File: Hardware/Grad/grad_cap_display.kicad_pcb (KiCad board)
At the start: 2 copper layers, 0 parts

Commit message: Start of modular PCB
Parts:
- added C1001: 1uF, New_Library:Worthington_C_0603, F.Cu at (-409.5, 120.0)
- added C1002: 22uF, New_Library:Worthington_C_0603, F.Cu at (-409.5, 122.5)
- added C1003: 1uF, New_Library:Worthington_C_0603, F.Cu at (-409.5, 125.0)
- added C1004: 22uF, New_Library:Worthington_C_0603, F.Cu at (-409.5, 127.5)
- added C1005: 100nF, New_Library:Worthington_C_0402, F.Cu at (-409.8, 149.9)
- added C1006: 22uF, New_Library:Worthington_C_0603, F.Cu at (-409.5, 130.0)
- added C1007: 100nF, New_Library:Worthington_C_0402, F.Cu at (-409.8, 152.1)
- added C1008: 100nF, New_Library:Worthington_C_0402, F.Cu at (-409.8, 154.3)
- added C1009: 100nF, New_Library:Worthington_C_0402, F.Cu at (-409.8, 156.5)
- added C1010: 100nF, New_Library:Worthington_C_0402, F.Cu at (-409.8, 158.7)
- added C1011: 100nF, New_Library:Worthington_C_0402, F.Cu at (-406.6, 149.9)
- added C1012: 22uF, New_Library:Worthington_D_0603, F.Cu at (-409.4, 135.0)
- added C1013: 100nF, New_Library:Worthington_C_0402, F.Cu at (-406.6, 152.1)
- added C1014: 100nF, New_Library:Worthington_C_0402, F.Cu at (-406.6, 154.3)
- added C1015: 22uF, New_Library:Worthington_C_0603, F.Cu at (-409.5, 132.5)
- added C1016: 100nF, New_Library:Worthington_C_0402, F.Cu at (-406.6, 156.5)
- added C1101: 100nF, Capacitor_SMD:C_0402_1005Metric, F.Cu at (-379.2, 157.2)
- added C1102: 22uF, Capacitor_SMD:C_0603_1608Metric, F.Cu at (-391.2, 160.4)
- added C1103: 22uF, Capacitor_SMD:C_0603_1608Metric, F.Cu at (-391.2, 163.0)
- added C1104: 100nF, Capacitor_SMD:C_0402_1005Metric, F.Cu at (-379.2, 159.2)
- added C1105: 100nF, Capacitor_SMD:C_0402_1005Metric, F.Cu at (-379.2, 161.2)
- added C1106: 22uF, Capacitor_SMD:C_0603_1608Metric, F.Cu at (-391.2, 165.5)
- added C201: 1uF, New_Library:Worthington_C_0603, F.Cu at (-268.5, 5.08)
- added C202: 22uF, New_Library:Worthington_C_0603, F.Cu at (-268.5, 7.58)
- added C203: 1uF, New_Library:Worthington_C_0603, F.Cu at (-268.5, 10.1)
- added C204: 22uF, New_Library:Worthington_C_0603, F.Cu at (-268.5, 12.6)
- added C205: 100nF, New_Library:Worthington_C_0402, F.Cu at (-268.8, 34.9)
- added C206: 22uF, New_Library:Worthington_C_0603, F.Cu at (-268.5, 15.1)
- added C207: 100nF, New_Library:Worthington_C_0402, F.Cu at (-268.8, 37.1)
- added C208: 100nF, New_Library:Worthington_C_0402, F.Cu at (-268.8, 39.3)
- added C209: 100nF, New_Library:Worthington_C_0402, F.Cu at (-268.8, 41.5)
- added C210: 100nF, New_Library:Worthington_C_0402, F.Cu at (-268.8, 43.7)
- added C211: 100nF, New_Library:Worthington_C_0402, F.Cu at (-265.6, 34.9)
- added C212: 22uF, New_Library:Worthington_D_0603, F.Cu at (-268.4, 20.1)
- added C213: 100nF, New_Library:Worthington_C_0402, F.Cu at (-265.6, 37.1)
- added C214: 100nF, New_Library:Worthington_C_0402, F.Cu at (-265.6, 39.3)
- added C215: 22uF, New_Library:Worthington_C_0603, F.Cu at (-268.5, 17.6)
- added C216: 100nF, New_Library:Worthington_C_0402, F.Cu at (-265.6, 41.5)
- added C301: 1uF, New_Library:Worthington_C_0603, F.Cu at (-409.5, 3.98)
- added C302: 22uF, New_Library:Worthington_C_0603, F.Cu at (-409.5, 6.49)
- added C303: 1uF, New_Library:Worthington_C_0603, F.Cu at (-409.5, 8.98)
- added C304: 22uF, New_Library:Worthington_C_0603, F.Cu at (-409.5, 11.5)
- added C305: 100nF, New_Library:Worthington_C_0402, F.Cu at (-409.8, 33.8)
- added C306: 22uF, New_Library:Worthington_C_0603, F.Cu at (-409.5, 14.0)
- added C307: 100nF, New_Library:Worthington_C_0402, F.Cu at (-409.8, 36.0)
- added C308: 100nF, New_Library:Worthington_C_0402, F.Cu at (-409.8, 38.2)
- added C309: 100nF, New_Library:Worthington_C_0402, F.Cu at (-409.8, 40.4)
- added C310: 100nF, New_Library:Worthington_C_0402, F.Cu at (-409.8, 42.6)
- added C311: 100nF, New_Library:Worthington_C_0402, F.Cu at (-406.6, 33.8)
- added C312: 22uF, New_Library:Worthington_D_0603, F.Cu at (-409.4, 19.0)
- added C313: 100nF, New_Library:Worthington_C_0402, F.Cu at (-406.6, 36.0)
- added C314: 100nF, New_Library:Worthington_C_0402, F.Cu at (-406.6, 38.2)
- added C315: 22uF, New_Library:Worthington_C_0603, F.Cu at (-409.5, 16.5)
- added C316: 100nF, New_Library:Worthington_C_0402, F.Cu at (-406.6, 40.4)
- added C401: 1uF, New_Library:Worthington_C_0603, F.Cu at (-409.5, 62.0)
- added C402: 22uF, New_Library:Worthington_C_0603, F.Cu at (-409.5, 64.5)
- added C403: 1uF, New_Library:Worthington_C_0603, F.Cu at (-409.5, 67.0)
- added C404: 22uF, New_Library:Worthington_C_0603, F.Cu at (-409.5, 69.5)
- added C405: 100nF, New_Library:Worthington_C_0402, F.Cu at (-409.8, 91.9)
- added C406: 22uF, New_Library:Worthington_C_0603, F.Cu at (-409.5, 72.0)
- added C407: 100nF, New_Library:Worthington_C_0402, F.Cu at (-409.8, 94.1)
- added C408: 100nF, New_Library:Worthington_C_0402, F.Cu at (-409.8, 96.3)
- added C409: 100nF, New_Library:Worthington_C_0402, F.Cu at (-409.8, 98.5)
- added C410: 100nF, New_Library:Worthington_C_0402, F.Cu at (-409.8, 100.7)
- added C411: 100nF, New_Library:Worthington_C_0402, F.Cu at (-406.6, 91.9)
- added C412: 22uF, New_Library:Worthington_D_0603, F.Cu at (-409.4, 77.0)
- added C413: 100nF, New_Library:Worthington_C_0402, F.Cu at (-406.6, 94.1)
- added C414: 100nF, New_Library:Worthington_C_0402, F.Cu at (-406.6, 96.3)
- added C415: 22uF, New_Library:Worthington_C_0603, F.Cu at (-409.5, 74.5)
- added C416: 100nF, New_Library:Worthington_C_0402, F.Cu at (-406.6, 98.5)
- added C501: 1uF, New_Library:Worthington_C_0603, F.Cu at (-467.0, 3.98)
- added C502: 22uF, New_Library:Worthington_C_0603, F.Cu at (-467.0, 6.49)
- added C503: 1uF, New_Library:Worthington_C_0603, F.Cu at (-467.0, 8.98)
- added C504: 22uF, New_Library:Worthington_C_0603, F.Cu at (-467.0, 11.5)
- added C505: 100nF, New_Library:Worthington_C_0402, F.Cu at (-467.3, 33.8)
- added C506: 22uF, New_Library:Worthington_C_0603, F.Cu at (-467.0, 14.0)
- added C507: 100nF, New_Library:Worthington_C_0402, F.Cu at (-467.3, 36.0)
- added C508: 100nF, New_Library:Worthington_C_0402, F.Cu at (-467.3, 38.2)
- added C509: 100nF, New_Library:Worthington_C_0402, F.Cu at (-467.3, 40.4)
- added C510: 100nF, New_Library:Worthington_C_0402, F.Cu at (-467.3, 42.6)
- added C511: 100nF, New_Library:Worthington_C_0402, F.Cu at (-464.1, 33.8)
- added C512: 22uF, New_Library:Worthington_D_0603, F.Cu at (-466.9, 19.0)
- added C513: 100nF, New_Library:Worthington_C_0402, F.Cu at (-464.1, 36.0)
- added C514: 100nF, New_Library:Worthington_C_0402, F.Cu at (-464.1, 38.2)
- added C515: 22uF, New_Library:Worthington_C_0603, F.Cu at (-467.0, 16.5)
- added C516: 100nF, New_Library:Worthington_C_0402, F.Cu at (-464.1, 40.4)
- added C601: 1uF, New_Library:Worthington_C_0603, F.Cu at (-524.4, 62.0)
- added C602: 22uF, New_Library:Worthington_C_0603, F.Cu at (-524.4, 64.5)
- added C603: 1uF, New_Library:Worthington_C_0603, F.Cu at (-524.4, 67.0)
- added C604: 22uF, New_Library:Worthington_C_0603, F.Cu at (-524.4, 69.5)
- added C605: 100nF, New_Library:Worthington_C_0402, F.Cu at (-524.7, 91.9)
- added C606: 22uF, New_Library:Worthington_C_0603, F.Cu at (-524.4, 72.0)
- added C607: 100nF, New_Library:Worthington_C_0402, F.Cu at (-524.7, 94.1)
- added C608: 100nF, New_Library:Worthington_C_0402, F.Cu at (-524.7, 96.3)
- added C609: 100nF, New_Library:Worthington_C_0402, F.Cu at (-524.7, 98.5)
- added C610: 100nF, New_Library:Worthington_C_0402, F.Cu at (-524.7, 100.7)
- added C611: 100nF, New_Library:Worthington_C_0402, F.Cu at (-521.5, 91.9)
- added C612: 22uF, New_Library:Worthington_D_0603, F.Cu at (-524.3, 77.0)
- added C613: 100nF, New_Library:Worthington_C_0402, F.Cu at (-521.5, 94.1)
- added C614: 100nF, New_Library:Worthington_C_0402, F.Cu at (-521.5, 96.3)
- added C615: 22uF, New_Library:Worthington_C_0603, F.Cu at (-524.4, 74.5)
- added C616: 100nF, New_Library:Worthington_C_0402, F.Cu at (-521.5, 98.5)
- added C701: 1uF, New_Library:Worthington_C_0603, F.Cu at (-467.0, 62.0)
- added C702: 22uF, New_Library:Worthington_C_0603, F.Cu at (-467.0, 64.5)
- added C703: 1uF, New_Library:Worthington_C_0603, F.Cu at (-467.0, 67.0)
- added C704: 22uF, New_Library:Worthington_C_0603, F.Cu at (-467.0, 69.5)
- added C705: 100nF, New_Library:Worthington_C_0402, F.Cu at (-467.3, 91.9)
- added C706: 22uF, New_Library:Worthington_C_0603, F.Cu at (-467.0, 72.0)
- added C707: 100nF, New_Library:Worthington_C_0402, F.Cu at (-467.3, 94.1)
- added C708: 100nF, New_Library:Worthington_C_0402, F.Cu at (-467.3, 96.3)
- added C709: 100nF, New_Library:Worthington_C_0402, F.Cu at (-467.3, 98.5)
- added C710: 100nF, New_Library:Worthington_C_0402, F.Cu at (-467.3, 100.7)
- added C711: 100nF, New_Library:Worthington_C_0402, F.Cu at (-464.1, 91.9)
- added C712: 22uF, New_Library:Worthington_D_0603, F.Cu at (-466.9, 77.0)
- added C713: 100nF, New_Library:Worthington_C_0402, F.Cu at (-464.1, 94.1)
- added C714: 100nF, New_Library:Worthington_C_0402, F.Cu at (-464.1, 96.3)
- added C715: 22uF, New_Library:Worthington_C_0603, F.Cu at (-467.0, 74.5)
- added C716: 100nF, New_Library:Worthington_C_0402, F.Cu at (-464.1, 98.5)
- added C801: 1uF, New_Library:Worthington_C_0603, F.Cu at (-467.0, 120.0)
- added C802: 22uF, New_Library:Worthington_C_0603, F.Cu at (-467.0, 122.5)
- added C803: 1uF, New_Library:Worthington_C_0603, F.Cu at (-467.0, 125.0)
- added C804: 22uF, New_Library:Worthington_C_0603, F.Cu at (-467.0, 127.5)
- added C805: 100nF, New_Library:Worthington_C_0402, F.Cu at (-467.3, 149.9)
- added C806: 22uF, New_Library:Worthington_C_0603, F.Cu at (-467.0, 130.0)
- added C807: 100nF, New_Library:Worthington_C_0402, F.Cu at (-467.3, 152.1)
- added C808: 100nF, New_Library:Worthington_C_0402, F.Cu at (-467.3, 154.3)
- added C809: 100nF, New_Library:Worthington_C_0402, F.Cu at (-467.3, 156.5)
- added C810: 100nF, New_Library:Worthington_C_0402, F.Cu at (-467.3, 158.7)
- added C811: 100nF, New_Library:Worthington_C_0402, F.Cu at (-464.1, 149.9)
- added C812: 22uF, New_Library:Worthington_D_0603, F.Cu at (-466.9, 135.0)
- added C813: 100nF, New_Library:Worthington_C_0402, F.Cu at (-464.1, 152.1)
- added C814: 100nF, New_Library:Worthington_C_0402, F.Cu at (-464.1, 154.3)
- added C815: 22uF, New_Library:Worthington_C_0603, F.Cu at (-467.0, 132.5)
- added C816: 100nF, New_Library:Worthington_C_0402, F.Cu at (-464.1, 156.5)
- added C901: 1uF, New_Library:Worthington_C_0603, F.Cu at (-524.4, 120.0)
- added C902: 22uF, New_Library:Worthington_C_0603, F.Cu at (-524.4, 122.5)
- added C903: 1uF, New_Library:Worthington_C_0603, F.Cu at (-524.4, 125.0)
- added C904: 22uF, New_Library:Worthington_C_0603, F.Cu at (-524.4, 127.5)
- added C905: 100nF, New_Library:Worthington_C_0402, F.Cu at (-524.7, 149.9)
- added C906: 22uF, New_Library:Worthington_C_0603, F.Cu at (-524.4, 130.0)
- added C907: 100nF, New_Library:Worthington_C_0402, F.Cu at (-524.7, 152.1)
- added C908: 100nF, New_Library:Worthington_C_0402, F.Cu at (-524.7, 154.3)
- added C909: 100nF, New_Library:Worthington_C_0402, F.Cu at (-524.7, 156.5)
- added C910: 100nF, New_Library:Worthington_C_0402, F.Cu at (-524.7, 158.7)
- added C911: 100nF, New_Library:Worthington_C_0402, F.Cu at (-521.5, 149.9)
- added C912: 22uF, New_Library:Worthington_D_0603, F.Cu at (-524.3, 135.0)
- added C913: 100nF, New_Library:Worthington_C_0402, F.Cu at (-521.5, 152.1)
- added C914: 100nF, New_Library:Worthington_C_0402, F.Cu at (-521.5, 154.3)
- added C915: 22uF, New_Library:Worthington_C_0603, F.Cu at (-524.4, 132.5)
- added C916: 100nF, New_Library:Worthington_C_0402, F.Cu at (-521.5, 156.5)
- added D1001: LED_Small, New_Library:Worthington_LED_0603, F.Cu at (-409.4, 137.5)
- added D1002: RED, New_Library:Worthington_LED_0603, F.Cu at (-409.4, 140.0)
- added D1003: RED, New_Library:Worthington_LED_0603, F.Cu at (-409.4, 142.5)
- added D1004: RED, New_Library:Worthington_LED_0603, F.Cu at (-409.4, 145.0)
- added D1005: RED, New_Library:Worthington_LED_0603, F.Cu at (-409.4, 147.5)
- added D1101: LED_Small, New_Library:Worthington_LED_0603, F.Cu at (-375.5, 162.8)
- added D1102: LED_Small, New_Library:Worthington_LED_0603, F.Cu at (-375.5, 165.3)
- added D201: LED_Small, New_Library:Worthington_LED_0603, F.Cu at (-268.4, 22.6)
- added D202: RED, New_Library:Worthington_LED_0603, F.Cu at (-268.4, 25.1)
- added D203: RED, New_Library:Worthington_LED_0603, F.Cu at (-268.4, 27.6)
- added D204: RED, New_Library:Worthington_LED_0603, F.Cu at (-268.4, 30.1)
- added D205: RED, New_Library:Worthington_LED_0603, F.Cu at (-268.4, 32.6)
- added D301: LED_Small, New_Library:Worthington_LED_0603, F.Cu at (-409.4, 21.5)
- added D302: RED, New_Library:Worthington_LED_0603, F.Cu at (-409.4, 24.0)
- added D303: RED, New_Library:Worthington_LED_0603, F.Cu at (-409.4, 26.5)
- added D304: RED, New_Library:Worthington_LED_0603, F.Cu at (-409.4, 29.0)
- added D305: RED, New_Library:Worthington_LED_0603, F.Cu at (-409.4, 31.5)
- added D401: LED_Small, New_Library:Worthington_LED_0603, F.Cu at (-409.4, 79.5)
- added D402: RED, New_Library:Worthington_LED_0603, F.Cu at (-409.4, 82.0)
- added D403: RED, New_Library:Worthington_LED_0603, F.Cu at (-409.4, 84.5)
- added D404: RED, New_Library:Worthington_LED_0603, F.Cu at (-409.4, 87.0)
- added D405: RED, New_Library:Worthington_LED_0603, F.Cu at (-409.4, 89.5)
- added D501: LED_Small, New_Library:Worthington_LED_0603, F.Cu at (-466.9, 21.5)
- added D502: RED, New_Library:Worthington_LED_0603, F.Cu at (-466.9, 24.0)
- added D503: RED, New_Library:Worthington_LED_0603, F.Cu at (-466.9, 26.5)
- added D504: RED, New_Library:Worthington_LED_0603, F.Cu at (-466.9, 29.0)
- added D505: RED, New_Library:Worthington_LED_0603, F.Cu at (-466.9, 31.5)
- added D601: LED_Small, New_Library:Worthington_LED_0603, F.Cu at (-524.3, 79.5)
- added D602: RED, New_Library:Worthington_LED_0603, F.Cu at (-524.3, 82.0)
- added D603: RED, New_Library:Worthington_LED_0603, F.Cu at (-524.3, 84.5)
- added D604: RED, New_Library:Worthington_LED_0603, F.Cu at (-524.3, 87.0)
- added D605: RED, New_Library:Worthington_LED_0603, F.Cu at (-524.3, 89.5)
- added D701: LED_Small, New_Library:Worthington_LED_0603, F.Cu at (-466.9, 79.5)
- added D702: RED, New_Library:Worthington_LED_0603, F.Cu at (-466.9, 82.0)
- added D703: RED, New_Library:Worthington_LED_0603, F.Cu at (-466.9, 84.5)
- added D704: RED, New_Library:Worthington_LED_0603, F.Cu at (-466.9, 87.0)
- added D705: RED, New_Library:Worthington_LED_0603, F.Cu at (-466.9, 89.5)
- added D801: LED_Small, New_Library:Worthington_LED_0603, F.Cu at (-466.9, 137.5)
- added D802: RED, New_Library:Worthington_LED_0603, F.Cu at (-466.9, 140.0)
- added D803: RED, New_Library:Worthington_LED_0603, F.Cu at (-466.9, 142.5)
- added D804: RED, New_Library:Worthington_LED_0603, F.Cu at (-466.9, 145.0)
- added D805: RED, New_Library:Worthington_LED_0603, F.Cu at (-466.9, 147.5)
- added D901: LED_Small, New_Library:Worthington_LED_0603, F.Cu at (-524.3, 137.5)
- added D902: RED, New_Library:Worthington_LED_0603, F.Cu at (-524.3, 140.0)
- added D903: RED, New_Library:Worthington_LED_0603, F.Cu at (-524.3, 142.5)
- added D904: RED, New_Library:Worthington_LED_0603, F.Cu at (-524.3, 145.0)
- added D905: RED, New_Library:Worthington_LED_0603, F.Cu at (-524.3, 147.5)
- added J1001: Amphenol 40-Pin FPC, New_Library:AMPHENOL_62684-402100ALF, F.Cu at (-446.6, 166.6)
- added J101: 6-Pos 2.54mm Header, Connector_PinHeader_2.54mm:PinHeader_1x06_P2.54mm_Vertical, F.Cu at (-400.7, 63.1)
- added J102: 6-Pos 2.54mm Header, Connector_PinHeader_2.54mm:PinHeader_1x06_P2.54mm_Vertical, F.Cu at (-396.1, 63.1)
- added J103: 6-Pos 2.54mm Header, Connector_PinHeader_2.54mm:PinHeader_1x06_P2.54mm_Vertical, F.Cu at (-391.6, 63.1)
- added J104: 6-Pos 2.54mm Header, Connector_PinHeader_2.54mm:PinHeader_1x06_P2.54mm_Vertical, F.Cu at (-387.0, 63.1)
- added J105: 6-Pos 2.54mm Header, Connector_PinHeader_2.54mm:PinHeader_1x06_P2.54mm_Vertical, F.Cu at (-382.4, 63.1)
- added J106: 6-Pos 2.54mm Header, Connector_PinHeader_2.54mm:PinHeader_1x06_P2.54mm_Vertical, F.Cu at (-377.8, 63.1)
- added J107: 6-Pos 2.54mm Header, Connector_PinHeader_2.54mm:PinHeader_1x06_P2.54mm_Vertical, F.Cu at (-373.2, 63.1)
- added J108: 6-Pos 2.54mm Header, Connector_PinHeader_2.54mm:PinHeader_1x06_P2.54mm_Vertical, F.Cu at (-368.6, 63.1)
- added J109: 6-Pos 2.54mm Header, Connector_PinHeader_2.54mm:PinHeader_1x06_P2.54mm_Vertical, F.Cu at (-364.0, 63.1)
- added J1101: JST-PH SPI, Connector_JST:JST_PH_S5B-PH-K_1x05_P2.00mm_Horizontal, F.Cu at (-400.1, 151.9)
- added J1102: JST-PH UART/I2C, Connector_JST:JST_PH_S6B-PH-K_1x06_P2.00mm_Horizontal, F.Cu at (-374.5, 144.6)
- added J1103: JST-PH A#, Connector_JST:JST_PH_S6B-PH-K_1x06_P2.00mm_Horizontal, F.Cu at (-374.5, 154.2)
- added J1104: Micro_SD_Card, New_Library:CUI_MSD-4-A, F.Cu at (-368.4, 128.6)
- added J201: Amphenol 40-Pin FPC, New_Library:AMPHENOL_62684-402100ALF, F.Cu at (-305.5, 51.6)
- added J301: Amphenol 40-Pin FPC, New_Library:AMPHENOL_62684-402100ALF, F.Cu at (-446.6, 50.5)
- added J401: Amphenol 40-Pin FPC, New_Library:AMPHENOL_62684-402100ALF, F.Cu at (-446.6, 108.5)
- added J501: Amphenol 40-Pin FPC, New_Library:AMPHENOL_62684-402100ALF, F.Cu at (-504.0, 50.5)
- added J601: Amphenol 40-Pin FPC, New_Library:AMPHENOL_62684-402100ALF, F.Cu at (-561.5, 108.5)
- added J701: Amphenol 40-Pin FPC, New_Library:AMPHENOL_62684-402100ALF, F.Cu at (-504.0, 108.5)
- added J801: Amphenol 40-Pin FPC, New_Library:AMPHENOL_62684-402100ALF, F.Cu at (-504.0, 166.6)
- added J901: Amphenol 40-Pin FPC, New_Library:AMPHENOL_62684-402100ALF, F.Cu at (-561.5, 166.6)
- added L1001: 22uH, New_Library:CDRH5D28, F.Cu at (-428.4, 165.3)
- added L201: 22uH, New_Library:CDRH5D28, F.Cu at (-287.3, 50.4)
- added L301: 22uH, New_Library:CDRH5D28, F.Cu at (-428.4, 49.3)
- added L401: 22uH, New_Library:CDRH5D28, F.Cu at (-428.4, 107.3)
- added L501: 22uH, New_Library:CDRH5D28, F.Cu at (-485.8, 49.3)
- added L601: 22uH, New_Library:CDRH5D28, F.Cu at (-543.3, 107.3)
- added L701: 22uH, New_Library:CDRH5D28, F.Cu at (-485.8, 107.3)
- added L801: 22uH, New_Library:CDRH5D28, F.Cu at (-485.8, 165.3)
- added L901: 22uH, New_Library:CDRH5D28, F.Cu at (-543.3, 165.3)
- added R1001: 430, New_Library:Worthington_R_0402, F.Cu at (-406.6, 158.7)
- added R1002: 10, Resistor_SMD:R_1210_3225Metric, F.Cu at (-457.7, 172.7)
- added R101: 120, New_Library:Worthington_R_0402, F.Cu at (-401.4, 79.2)
- added R102: 120, New_Library:Worthington_R_0402, F.Cu at (-401.4, 81.4)
- added R1101: 1k, New_Library:Worthington_R_0402, F.Cu at (-367.2, 162.6)
- added R1102: 430, New_Library:Worthington_R_0402, F.Cu at (-367.2, 164.8)
- added R201: 430, New_Library:Worthington_R_0402, F.Cu at (-265.6, 43.7)
- added R202: 10, Resistor_SMD:R_1210_3225Metric, F.Cu at (-316.6, 57.8)
- added R301: 430, New_Library:Worthington_R_0402, F.Cu at (-406.6, 42.6)
- added R302: 10, Resistor_SMD:R_1210_3225Metric, F.Cu at (-457.7, 56.7)
- added R401: 430, New_Library:Worthington_R_0402, F.Cu at (-406.6, 100.7)
- added R402: 10, Resistor_SMD:R_1210_3225Metric, F.Cu at (-457.7, 114.7)
- added R501: 430, New_Library:Worthington_R_0402, F.Cu at (-464.1, 42.6)
- added R502: 10, Resistor_SMD:R_1210_3225Metric, F.Cu at (-515.1, 56.7)
- added R601: 430, New_Library:Worthington_R_0402, F.Cu at (-521.5, 100.7)
- added R602: 10, Resistor_SMD:R_1210_3225Metric, F.Cu at (-572.6, 114.7)
- added R701: 430, New_Library:Worthington_R_0402, F.Cu at (-464.1, 100.7)
- added R702: 10, Resistor_SMD:R_1210_3225Metric, F.Cu at (-515.1, 114.7)
- added R801: 430, New_Library:Worthington_R_0402, F.Cu at (-464.1, 158.7)
- added R802: 10, Resistor_SMD:R_1210_3225Metric, F.Cu at (-515.1, 172.7)
- added R901: 430, New_Library:Worthington_R_0402, F.Cu at (-521.5, 158.7)
- added R902: 10, Resistor_SMD:R_1210_3225Metric, F.Cu at (-572.6, 172.7)
- added RN1001: 10k, New_Library:RESCAXE80P320X160X70-8N, F.Cu at (-412.4, 170.0)
- added RN1002: 430, New_Library:RESCAXE80P320X160X70-8N, F.Cu at (-407.6, 170.0)
- added RN1101: 47k, New_Library:RESCAXE80P320X160X70-8N, F.Cu at (-370.9, 163.9)
- added RN201: 10k, New_Library:RESCAXE80P320X160X70-8N, F.Cu at (-271.4, 55.1)
- added RN202: 430, New_Library:RESCAXE80P320X160X70-8N, F.Cu at (-266.6, 55.1)
- added RN301: 10k, New_Library:RESCAXE80P320X160X70-8N, F.Cu at (-412.4, 54.0)
- added RN302: 430, New_Library:RESCAXE80P320X160X70-8N, F.Cu at (-407.6, 54.0)
- added RN401: 10k, New_Library:RESCAXE80P320X160X70-8N, F.Cu at (-412.4, 112.0)
- added RN402: 430, New_Library:RESCAXE80P320X160X70-8N, F.Cu at (-407.6, 112.0)
- added RN501: 10k, New_Library:RESCAXE80P320X160X70-8N, F.Cu at (-469.9, 54.0)
- added RN502: 430, New_Library:RESCAXE80P320X160X70-8N, F.Cu at (-465.1, 54.0)
- added RN601: 10k, New_Library:RESCAXE80P320X160X70-8N, F.Cu at (-527.3, 112.0)
- added RN602: 430, New_Library:RESCAXE80P320X160X70-8N, F.Cu at (-522.5, 112.0)
- added RN701: 10k, New_Library:RESCAXE80P320X160X70-8N, F.Cu at (-469.9, 112.0)
- added RN702: 430, New_Library:RESCAXE80P320X160X70-8N, F.Cu at (-465.1, 112.0)
- added RN801: 10k, New_Library:RESCAXE80P320X160X70-8N, F.Cu at (-469.9, 170.0)
- added RN802: 430, New_Library:RESCAXE80P320X160X70-8N, F.Cu at (-465.1, 170.0)
- added RN901: 10k, New_Library:RESCAXE80P320X160X70-8N, F.Cu at (-527.3, 170.0)
- added RN902: 430, New_Library:RESCAXE80P320X160X70-8N, F.Cu at (-522.5, 170.0)
- added U1001: LM66200DRLR, Package_TO_SOT_SMD:SOT-583-8, F.Cu at (-453.0, 172.6)
- added U1002: TLV75733PDRV, Package_SON:WSON-6-1EP_2x2mm_P0.65mm_EP1x1.6mm, F.Cu at (-443.7, 172.5)
- added U1003: SN74LVC1G139, Package_SO:VSSOP-8_2.3x2mm_P0.5mm, F.Cu at (-448.4, 172.6)
- added U1004: ESP32-S3-WROOM-1-N8R8, RF_Module:ESP32-S3-WROOM-1, F.Cu at (-436.0, 147.1)
- added U1005: TC7MBL3126CFT, Package_SO:TSSOP-14_4.4x5mm_P0.65mm, F.Cu at (-419.5, 164.5)
- added U1006: AP3019AKTTR, Package_TO_SOT_SMD:TSOT-23-6, F.Cu at (-430.1, 172.0)
- added U1007: W25Q128JVP, Package_SON:WSON-8-1EP_6x5mm_P1.27mm_EP3.4x4.3mm, F.Cu at (-410.9, 164.3)
- added U1008: THVD1400D, Package_SO:SOIC-8_3.9x4.9mm_P1.27mm, F.Cu at (-419.6, 171.1)
- added U1101: TC7MBL3126CFT, Package_SO:TSSOP-14_4.4x5mm_P0.65mm, F.Cu at (-384.7, 153.0)
- added U1102: AZ1117-5.0, Package_TO_SOT_SMD:SOT-223-3_TabPin2, F.Cu at (-398.1, 163.4)
- added U1103: THVD1400D, Package_SO:SOIC-8_3.9x4.9mm_P1.27mm, F.Cu at (-384.9, 159.6)
- added U1104: QTPy SAMD21, New_Library:Py_QT_SAMD21, F.Cu at (-390.3, 137.7)
- added U201: LM66200DRLR, Package_TO_SOT_SMD:SOT-583-8, F.Cu at (-312.0, 57.6)
- added U202: TLV75733PDRV, Package_SON:WSON-6-1EP_2x2mm_P0.65mm_EP1x1.6mm, F.Cu at (-302.7, 57.5)
- added U203: SN74LVC1G139, Package_SO:VSSOP-8_2.3x2mm_P0.5mm, F.Cu at (-307.3, 57.6)
- added U204: ESP32-S3-WROOM-1-N8R8, RF_Module:ESP32-S3-WROOM-1, F.Cu at (-294.9, 32.1)
- added U205: TC7MBL3126CFT, Package_SO:TSSOP-14_4.4x5mm_P0.65mm, F.Cu at (-278.4, 49.5)
- added U206: AP3019AKTTR, Package_TO_SOT_SMD:TSOT-23-6, F.Cu at (-289.0, 57.0)
- added U207: W25Q128JVP, Package_SON:WSON-8-1EP_6x5mm_P1.27mm_EP3.4x4.3mm, F.Cu at (-269.8, 49.4)
- added U208: THVD1400D, Package_SO:SOIC-8_3.9x4.9mm_P1.27mm, F.Cu at (-278.6, 56.1)
- added U301: LM66200DRLR, Package_TO_SOT_SMD:SOT-583-8, F.Cu at (-453.0, 56.6)
- added U302: TLV75733PDRV, Package_SON:WSON-6-1EP_2x2mm_P0.65mm_EP1x1.6mm, F.Cu at (-443.7, 56.4)
- added U303: SN74LVC1G139, Package_SO:VSSOP-8_2.3x2mm_P0.5mm, F.Cu at (-448.4, 56.5)
- added U304: ESP32-S3-WROOM-1-N8R8, RF_Module:ESP32-S3-WROOM-1, F.Cu at (-436.0, 31.0)
- added U305: TC7MBL3126CFT, Package_SO:TSSOP-14_4.4x5mm_P0.65mm, F.Cu at (-419.5, 48.4)
- added U306: AP3019AKTTR, Package_TO_SOT_SMD:TSOT-23-6, F.Cu at (-430.1, 55.9)
- added U307: W25Q128JVP, Package_SON:WSON-8-1EP_6x5mm_P1.27mm_EP3.4x4.3mm, F.Cu at (-410.9, 48.3)
- added U308: THVD1400D, Package_SO:SOIC-8_3.9x4.9mm_P1.27mm, F.Cu at (-419.6, 55.1)
- added U401: LM66200DRLR, Package_TO_SOT_SMD:SOT-583-8, F.Cu at (-453.0, 114.6)
- added U402: TLV75733PDRV, Package_SON:WSON-6-1EP_2x2mm_P0.65mm_EP1x1.6mm, F.Cu at (-443.7, 114.5)
- added U403: SN74LVC1G139, Package_SO:VSSOP-8_2.3x2mm_P0.5mm, F.Cu at (-448.4, 114.5)
- added U404: ESP32-S3-WROOM-1-N8R8, RF_Module:ESP32-S3-WROOM-1, F.Cu at (-436.0, 89.0)
- added U405: TC7MBL3126CFT, Package_SO:TSSOP-14_4.4x5mm_P0.65mm, F.Cu at (-419.5, 106.5)
- added U406: AP3019AKTTR, Package_TO_SOT_SMD:TSOT-23-6, F.Cu at (-430.1, 114.0)
- added U407: W25Q128JVP, Package_SON:WSON-8-1EP_6x5mm_P1.27mm_EP3.4x4.3mm, F.Cu at (-410.9, 106.3)
- added U408: THVD1400D, Package_SO:SOIC-8_3.9x4.9mm_P1.27mm, F.Cu at (-419.6, 113.1)
- added U501: LM66200DRLR, Package_TO_SOT_SMD:SOT-583-8, F.Cu at (-510.5, 56.6)
- added U502: TLV75733PDRV, Package_SON:WSON-6-1EP_2x2mm_P0.65mm_EP1x1.6mm, F.Cu at (-501.2, 56.4)
- added U503: SN74LVC1G139, Package_SO:VSSOP-8_2.3x2mm_P0.5mm, F.Cu at (-505.8, 56.5)
- added U504: ESP32-S3-WROOM-1-N8R8, RF_Module:ESP32-S3-WROOM-1, F.Cu at (-493.4, 31.0)
- added U505: TC7MBL3126CFT, Package_SO:TSSOP-14_4.4x5mm_P0.65mm, F.Cu at (-476.9, 48.4)
- added U506: AP3019AKTTR, Package_TO_SOT_SMD:TSOT-23-6, F.Cu at (-487.5, 55.9)
- added U507: W25Q128JVP, Package_SON:WSON-8-1EP_6x5mm_P1.27mm_EP3.4x4.3mm, F.Cu at (-468.3, 48.3)
- added U508: THVD1400D, Package_SO:SOIC-8_3.9x4.9mm_P1.27mm, F.Cu at (-477.1, 55.1)
- added U601: LM66200DRLR, Package_TO_SOT_SMD:SOT-583-8, F.Cu at (-567.9, 114.6)
- added U602: TLV75733PDRV, Package_SON:WSON-6-1EP_2x2mm_P0.65mm_EP1x1.6mm, F.Cu at (-558.6, 114.5)
- added U603: SN74LVC1G139, Package_SO:VSSOP-8_2.3x2mm_P0.5mm, F.Cu at (-563.3, 114.5)
- added U604: ESP32-S3-WROOM-1-N8R8, RF_Module:ESP32-S3-WROOM-1, F.Cu at (-550.9, 89.0)
- added U605: TC7MBL3126CFT, Package_SO:TSSOP-14_4.4x5mm_P0.65mm, F.Cu at (-534.4, 106.5)
- added U606: AP3019AKTTR, Package_TO_SOT_SMD:TSOT-23-6, F.Cu at (-545.0, 114.0)
- added U607: W25Q128JVP, Package_SON:WSON-8-1EP_6x5mm_P1.27mm_EP3.4x4.3mm, F.Cu at (-525.8, 106.3)
- added U608: THVD1400D, Package_SO:SOIC-8_3.9x4.9mm_P1.27mm, F.Cu at (-534.5, 113.1)
- added U701: LM66200DRLR, Package_TO_SOT_SMD:SOT-583-8, F.Cu at (-510.5, 114.6)
- added U702: TLV75733PDRV, Package_SON:WSON-6-1EP_2x2mm_P0.65mm_EP1x1.6mm, F.Cu at (-501.2, 114.5)
- added U703: SN74LVC1G139, Package_SO:VSSOP-8_2.3x2mm_P0.5mm, F.Cu at (-505.8, 114.5)
- added U704: ESP32-S3-WROOM-1-N8R8, RF_Module:ESP32-S3-WROOM-1, F.Cu at (-493.4, 89.0)
- added U705: TC7MBL3126CFT, Package_SO:TSSOP-14_4.4x5mm_P0.65mm, F.Cu at (-476.9, 106.5)
- added U706: AP3019AKTTR, Package_TO_SOT_SMD:TSOT-23-6, F.Cu at (-487.5, 114.0)
- added U707: W25Q128JVP, Package_SON:WSON-8-1EP_6x5mm_P1.27mm_EP3.4x4.3mm, F.Cu at (-468.3, 106.3)
- added U708: THVD1400D, Package_SO:SOIC-8_3.9x4.9mm_P1.27mm, F.Cu at (-477.1, 113.1)
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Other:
- board outline added: 274.7 x 276.5 mm

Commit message: Prototype of PCB layout
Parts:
- removed C1001, C1003, C301, C303, C401, C403, C501, C503, C601, C603, C701, C703, C801, C803, C901, C903: 1uF, New_Library:Worthington_C_0603
- removed C1002, C1004, C1006, C1015, C302, C304, C306, C315, C402, C404, C406, C415, C502, C504, C506, C515, C602, C604, C606, C615, C702, C704, C706, C715, C802, C804, C806, C815, C902, C904, C906, C915: 22uF, New_Library:Worthington_C_0603
- removed C1005, C1007, C1008, C1009, C1010, C1011, C1013, C1014, C1016, C305, C307, C308, C309, C310, C311, C313, C314, C316, C405, C407, C408, C409, C410, C411, C413, C414, C416, C505, C507, C508, C509, C510, C511, C513, C514, C516, C605, C607, C608, C609, C610, C611, C613, C614, C616, C705, C707, C708, C709, C710, C711, C713, C714, C716, C805, C807, C808, C809, C810, C811, C813, C814, C816, C905, C907, C908, C909, C910, C911, C913, C914, C916: 100nF, New_Library:Worthington_C_0402
- removed C1012, C312, C412, C512, C612, C712, C812, C912: 22uF, New_Library:Worthington_D_0603
- removed D1001, D301, D401, D501, D601, D701, D801, D901: LED_Small, New_Library:Worthington_LED_0603
- removed D1002, D1003, D1004, D1005, D302, D303, D304, D305, D402, D403, D404, D405, D502, D503, D504, D505, D602, D603, D604, D605, D702, D703, D704, D705, D802, D803, D804, D805, D902, D903, D904, D905: RED, New_Library:Worthington_LED_0603
- removed J1001, J301, J401, J501, J601, J701, J801, J901: Amphenol 40-Pin FPC, New_Library:AMPHENOL_62684-402100ALF
- removed J102, J103, J104, J105, J106, J107, J108, J109: 6-Pos 2.54mm Header, Connector_PinHeader_2.54mm:PinHeader_1x06_P2.54mm_Vertical
- removed L1001, L301, L401, L501, L601, L701, L801, L901: 22uH, New_Library:CDRH5D28
- removed R1001, R301, R401, R501, R601, R701, R801, R901: 430, New_Library:Worthington_R_0402
- removed R1002, R302, R402, R502, R602, R702, R802, R902: 10, Resistor_SMD:R_1210_3225Metric
- removed R101, R102: 120, New_Library:Worthington_R_0402
- removed RN1001, RN301, RN401, RN501, RN601, RN701, RN801, RN901: 10k, New_Library:RESCAXE80P320X160X70-8N
- removed RN1002, RN302, RN402, RN502, RN602, RN702, RN802, RN902: 430, New_Library:RESCAXE80P320X160X70-8N
- removed U1001, U301, U401, U501, U601, U701, U801, U901: LM66200DRLR, Package_TO_SOT_SMD:SOT-583-8
- removed U1002, U302, U402, U502, U602, U702, U802, U902: TLV75733PDRV, Package_SON:WSON-6-1EP_2x2mm_P0.65mm_EP1x1.6mm
- removed U1003, U303, U403, U503, U603, U703, U803, U903: SN74LVC1G139, Package_SO:VSSOP-8_2.3x2mm_P0.5mm
- removed U1004, U304, U404, U504, U604, U704, U804, U904: ESP32-S3-WROOM-1-N8R8, RF_Module:ESP32-S3-WROOM-1
- removed U1005, U305, U405, U505, U605, U705, U805, U905: TC7MBL3126CFT, Package_SO:TSSOP-14_4.4x5mm_P0.65mm
- removed U1006, U306, U406, U506, U606, U706, U806, U906: AP3019AKTTR, Package_TO_SOT_SMD:TSOT-23-6
- removed U1007, U307, U407, U507, U607, U707, U807, U907: W25Q128JVP, Package_SON:WSON-8-1EP_6x5mm_P1.27mm_EP3.4x4.3mm
- removed U1008, U308, U408, U508, U608, U708, U808, U908: THVD1400D, Package_SO:SOIC-8_3.9x4.9mm_P1.27mm
- added J202: 01x30 Pads, Connector_PinSocket_2.54mm:PinSocket_1x30_P2.54mm_Vertical, F.Cu at (-269.6, -672.8)
- added J203: 01x30 Pads, Connector_PinSocket_2.54mm:PinSocket_1x30_P2.54mm_Vertical, F.Cu at (-268.1, -674.3)
- added J204: 01x30 Pads, Connector_PinSocket_2.54mm:PinSocket_1x30_P2.54mm_Vertical, F.Cu at (-193.1, -599.2)
- added J205: 01x30 Pads, Connector_PinSocket_2.54mm:PinSocket_1x30_P2.54mm_Vertical, F.Cu at (-194.5, -597.8)
- added J3: 2x8 2.54mm IDC Header, Connector_IDC:IDC-Header_2x06_P2.54mm_Vertical_SMD, F.Cu at (-231.4, -638.8)
- added R203: 120, New_Library:Worthington_R_0402, F.Cu at (-212.0, -647.7)
- added R204: 120, New_Library:Worthington_R_0402, F.Cu at (-253.7, -657.4)
- D201: value LED_Small -> RED
- J101: footprint Connector_PinHeader_2.54mm:PinHeader_1x06_P2.54mm_Vertical -> Connector_PinHeader_2.54mm:PinHeader_1x06_P2.54mm_Vertical_SMD_Pin1Left
- moved U1103 832.2 mm to (-253.6, -662.2), turned to -90 degrees
- moved R1102 824.5 mm to (-261.6, -652.9), turned to 90 degrees
- moved D1102 823.5 mm to (-261.6, -650.3), turned to -90 degrees
- moved R1101 822.1 mm to (-263.5, -652.9), turned to 90 degrees
- moved D1101 820.7 mm to (-263.5, -650.3), turned to -90 degrees
- moved C1101 815.9 mm to (-260.2, -649.9), turned to 90 degrees
- moved C1106 810.9 mm to (-210.0, -624.9)
- moved RN1101 806.7 mm to (-205.7, -625.7), turned to 90 degrees
- moved C1105 805.3 mm to (-210.0, -626.2)
- moved U1102 792.8 mm to (-253.2, -616.1)
- moved U1104 785.1 mm to (-257.3, -636.1), turned to 90 degrees
- moved C1103 785.0 mm to (-256.9, -610.5), turned to -90 degrees
- moved C1102 782.8 mm to (-255.3, -610.5), turned to -90 degrees
- moved J1104 782.2 mm to (-203.9, -636.1), turned to 90 degrees
- moved C1104 779.3 mm to (-258.1, -610.6), turned to -90 degrees
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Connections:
- net /PROG_ESP1_EN renamed /ESP32 1/ESP_PROG_EN
- net /PROG_ESP1_IO0 renamed /ESP32 1/ESP_PROG_IO0
- net /PROG_ESP1_PWR renamed /ESP32 1/ESP_PROG_PWR
- net /PROG_ESP1_RXD0 renamed /ESP32 1/ESP_PROG_RXD0
- net /PROG_ESP1_TXD0 renamed /ESP32 1/ESP_PROG_TXD0
- net /RS485_A renamed /ESP32 1/RS485_A
- net /SAMD21/SAMD21_3V3 renamed /ESP32 1/SAMD21_3V3
- net /SAMD21/SAMD21_5V renamed /ESP32 1/SAMD21_5V
- net /SAMD21/SAMD_MISO renamed /ESP32 1/SAMD_MISO
- net /SAMD21/SAMD_MOSI renamed /ESP32 1/SAMD_MOSI
- net /SAMD21/SAMD_SCK renamed /ESP32 1/SAMD_SCK
- net /SAMD21/SAMD_SDA renamed /ESP32 1/SAMD_SDA
- net /SAMD21/SPI_MISO_µSD renamed /ESP32 1/SPI_MISO_µSD
- net /SAMD21/SPI_MOSI_µSD renamed /ESP32 1/SPI_MOSI_µSD
- net /SAMD21/SPI_SCK_µSD renamed /ESP32 1/SPI_SCK_µSD
- C1102 pad 1: /SAMD21/PWR_IN -> /ESP32 1/BATT_IN
- D202 pad 1: Net-(D202-K) -> GND
- D202 pad 2: /ESP32 1/SPI_µSD_BUS_CONNECT -> Net-(D202-A)
- D203 pad 1: Net-(D203-K) -> GND
- D203 pad 2: /ESP32 1/SPI_CS_µSD -> Net-(D203-A)
- D204 pad 1: Net-(D204-K) -> GND
- D204 pad 2: /ESP32 1/SPI_CS_FLASH -> Net-(D204-A)
- D205 pad 1: Net-(D205-K) -> GND
- D205 pad 2: /ESP32 1/SPI_CS_LCD -> Net-(D205-A)
- J1102 pad 3: /SAMD21/BACKLIGHT_PWM -> /ESP32 1/BACKLIGHT_PWM
- J1102 pad 4: /SAMD21/UART-RS485_TX -> /ESP32 1/UART-RS485_TX
- J1102 pad 5: /SAMD21/UART-RS485_RX -> /ESP32 1/UART-RS485_RX
- J1103 pad 2: /SAMD21/SPI_µSD_BUS_CONNECT -> /ESP32 1/SPI_µSD_BUS_CONNECT
- J1103 pad 4: /FRAME_SYNC -> /ESP32 1/FRAME_SYNC
- J1103 pad 5: /SAMD21/UART_RS485_DE -> /ESP32 1/UART_RS485_DE
- RN201 pad 5: /ESP32 1/SPI_CS_LCD -> /ESP32 1/SPI_CS_µSD
- RN201 pad 7: /ESP32 1/SPI_CS_µSD -> /ESP32 1/SPI_CS_LCD
- RN202 pad 1: Net-(D202-K) -> Net-(D202-A)
- RN202 pad 2: Net-(D203-K) -> Net-(D203-A)
- RN202 pad 3: Net-(D204-K) -> Net-(D204-A)
- RN202 pad 4: Net-(D205-K) -> Net-(D205-A)
- RN202 pad 5: GND -> /ESP32 1/SPI_CS_LCD
- RN202 pad 6: GND -> /ESP32 1/SPI_CS_FLASH
- RN202 pad 7: GND -> /ESP32 1/SPI_CS_µSD
- RN202 pad 8: GND -> /ESP32 1/SPI_µSD_BUS_CONNECT
- U1101 pad 1: /SAMD21/SPI_µSD_BUS_CONNECT -> /ESP32 1/SPI_µSD_BUS_CONNECT
- U1101 pad 10: /SAMD21/SPI_µSD_BUS_CONNECT -> /ESP32 1/SPI_µSD_BUS_CONNECT
- U1101 pad 13: /SAMD21/SPI_µSD_BUS_CONNECT -> /ESP32 1/SPI_µSD_BUS_CONNECT
- U1101 pad 4: /SAMD21/SPI_µSD_BUS_CONNECT -> /ESP32 1/SPI_µSD_BUS_CONNECT
- U1102 pad 3: /SAMD21/PWR_IN -> /ESP32 1/BATT_IN
- U1103 pad 1: /SAMD21/UART-RS485_RX -> /ESP32 1/UART-RS485_RX
- U1103 pad 2: /SAMD21/UART_RS485_DE -> /ESP32 1/UART_RS485_DE
- U1103 pad 3: /SAMD21/UART_RS485_DE -> /ESP32 1/UART_RS485_DE
- U1103 pad 4: /SAMD21/UART-RS485_TX -> /ESP32 1/UART-RS485_TX
- U1103 pad 7: /FRAME_SYNC -> /ESP32 1/RS485_B
- U1104 pad 1: /SAMD21/SPI_µSD_BUS_CONNECT -> /ESP32 1/SPI_µSD_BUS_CONNECT
- U1104 pad 3: /FRAME_SYNC -> /ESP32 1/FRAME_SYNC
- U1104 pad 4: /SAMD21/UART_RS485_DE -> /ESP32 1/UART_RS485_DE
- U1104 pad 6: /SAMD21/BACKLIGHT_PWM -> /ESP32 1/BACKLIGHT_PWM
- U1104 pad 7: /SAMD21/UART-RS485_TX -> /ESP32 1/UART-RS485_TX
- U1104 pad 8: /SAMD21/UART-RS485_RX -> /ESP32 1/UART-RS485_RX
- U204 pad 39: /FRAME_SYNC -> /ESP32 1/FRAME_SYNC
- U206 pad 4: /SAMD21/BACKLIGHT_PWM -> /ESP32 1/BACKLIGHT_PWM_IN
- U207 pad 4: unconnected-(U207-GND-Pad4) -> GND
- U208 pad 7: /FRAME_SYNC -> /ESP32 1/RS485_B
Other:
- board size 274.7 x 276.5 mm -> 76.5 x 76.5 mm
- copper layers 2 -> 4

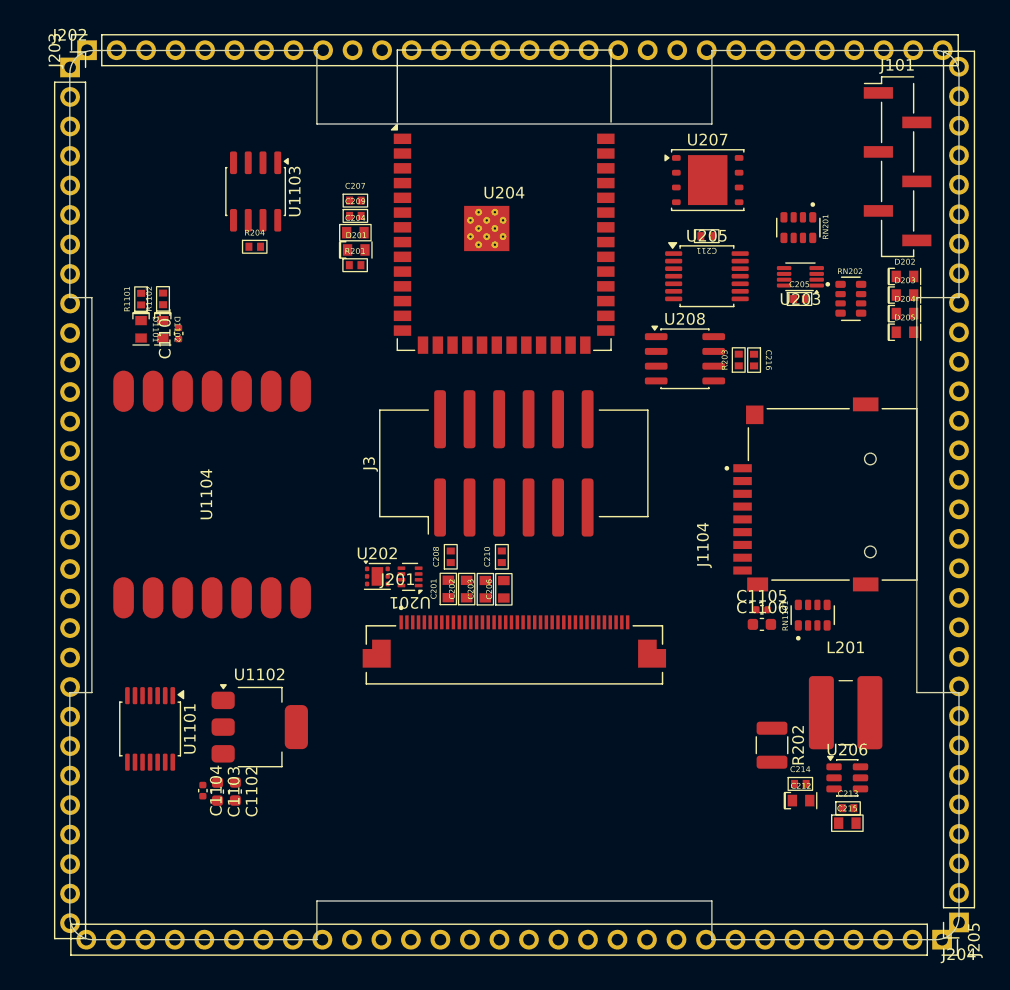
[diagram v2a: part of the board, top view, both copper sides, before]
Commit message: Fixed flipped FPC connector pinout
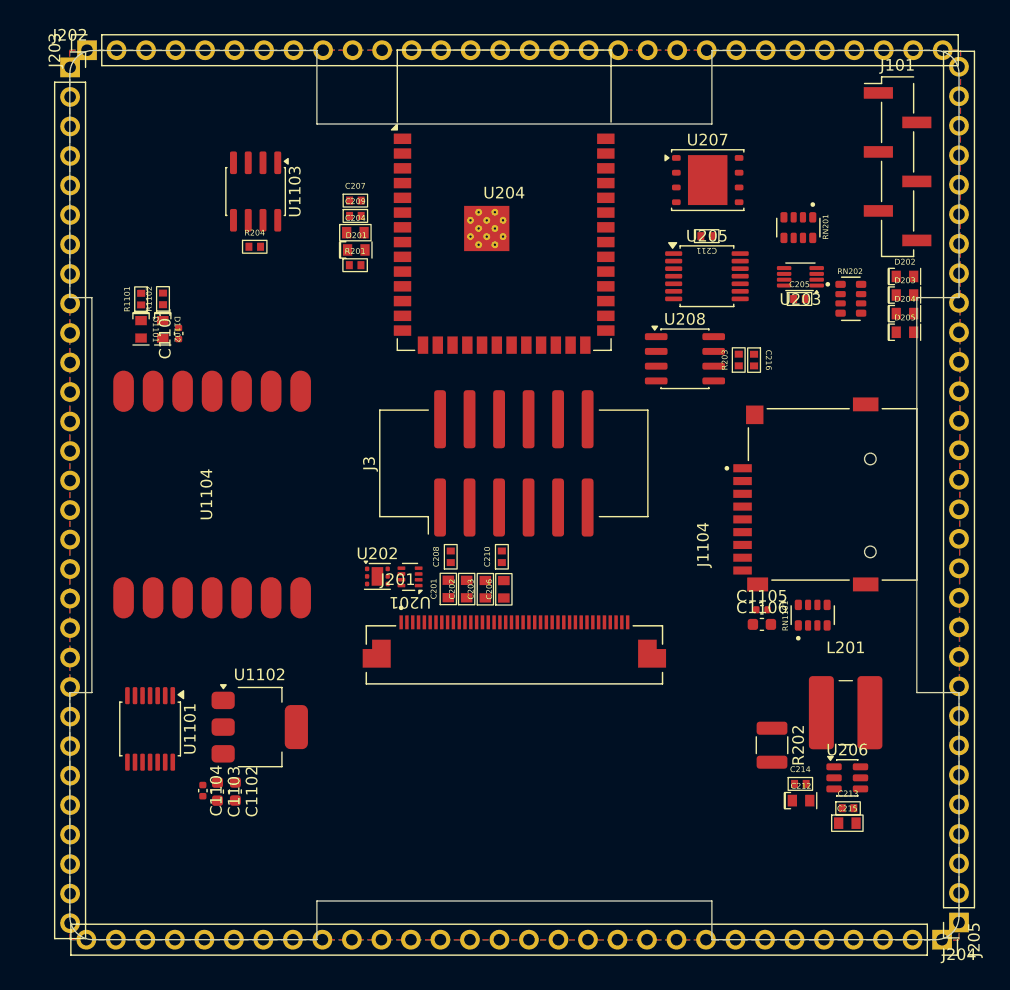
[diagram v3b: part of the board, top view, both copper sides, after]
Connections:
- J201 pad 1: Net-(J201-LEDA) -> GND
- J201 pad 10: /ESP32 1/SPI_SCK -> /ESP32 1/LCD_RGB_DB15
- J201 pad 11: /ESP32 1/SPI_CS_LCD -> /ESP32 1/LCD_RGB_DB14
- J201 pad 12: /ESP32 1/LCD_RGB_PCLK -> /ESP32 1/LCD_RGB_DB13
- J201 pad 13: /ESP32 1/LCD_RGB_DE -> /ESP32 1/LCD_RGB_DB12
- J201 pad 14: /ESP32 1/LCD_RGB_VSYNC -> /ESP32 1/LCD_RGB_DB11
- J201 pad 15: /ESP32 1/LCD_RGB_HSYNC -> /ESP32 1/LCD_RGB_DB10
- J201 pad 16: /ESP32 1/LCD_RGB_DB0 -> /ESP32 1/LCD_RGB_DB9
- J201 pad 17: /ESP32 1/LCD_RGB_DB1 -> /ESP32 1/LCD_RGB_DB8
- J201 pad 18: /ESP32 1/LCD_RGB_DB2 -> /ESP32 1/LCD_RGB_DB7
- J201 pad 19: /ESP32 1/LCD_RGB_DB3 -> /ESP32 1/LCD_RGB_DB6
- J201 pad 2: Net-(U206-FB) -> unconnected-(J201-TP-VCL-Pad2)
- J201 pad 20: /ESP32 1/LCD_RGB_DB4 -> /ESP32 1/LCD_RGB_DB5
- J201 pad 21: /ESP32 1/LCD_RGB_DB5 -> /ESP32 1/LCD_RGB_DB4
- J201 pad 22: /ESP32 1/LCD_RGB_DB6 -> /ESP32 1/LCD_RGB_DB3
- J201 pad 23: /ESP32 1/LCD_RGB_DB7 -> /ESP32 1/LCD_RGB_DB2
- J201 pad 24: /ESP32 1/LCD_RGB_DB8 -> /ESP32 1/LCD_RGB_DB1
- J201 pad 25: /ESP32 1/LCD_RGB_DB9 -> /ESP32 1/LCD_RGB_DB0
- J201 pad 26: /ESP32 1/LCD_RGB_DB10 -> /ESP32 1/LCD_RGB_HSYNC
- J201 pad 27: /ESP32 1/LCD_RGB_DB11 -> /ESP32 1/LCD_RGB_VSYNC
- J201 pad 28: /ESP32 1/LCD_RGB_DB12 -> /ESP32 1/LCD_RGB_DE
- J201 pad 29: /ESP32 1/LCD_RGB_DB13 -> /ESP32 1/LCD_RGB_PCLK
- J201 pad 3: Net-(U206-FB) -> unconnected-(J201-TP-RST-Pad3)
- J201 pad 30: /ESP32 1/LCD_RGB_DB14 -> /ESP32 1/SPI_CS_LCD
- J201 pad 31: /ESP32 1/LCD_RGB_DB15 -> /ESP32 1/SPI_SCK
- J201 pad 32: /ESP32 1/LCD_RGB_DB16 -> /ESP32 1/SPI_MOSI
- J201 pad 33: /ESP32 1/LCD_RGB_DB17 -> unconnected-(J201-NC-Pad33)
- J201 pad 34: GND -> unconnected-(J201-NC-Pad34)
- J201 pad 36: unconnected-(J201-TP-SDA-Pad36) -> /ESP32 1/+3V3
- J201 pad 37: unconnected-(J201-TP-SCL-Pad37) -> GND
- J201 pad 38: unconnected-(J201-TP-RST-Pad38) -> Net-(U206-FB)
- J201 pad 39: unconnected-(J201-TP-VCL-Pad39) -> Net-(U206-FB)
- J201 pad 4: GND -> unconnected-(J201-TP-SCL-Pad4)
- J201 pad 40: GND -> Net-(J201-LEDA)
- J201 pad 5: /ESP32 1/+3V3 -> unconnected-(J201-TP-SDA-Pad5)
- J201 pad 7: unconnected-(J201-NC-Pad7) -> GND
- J201 pad 8: unconnected-(J201-NC-Pad8) -> /ESP32 1/LCD_RGB_DB17
- J201 pad 9: /ESP32 1/SPI_MOSI -> /ESP32 1/LCD_RGB_DB16
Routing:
- added copper zone on In2.Cu, net /ESP32 1/+3V3
- added copper zone on B.Cu, net GND
- added copper zone on F.Cu, net GND
- added copper zone on In1.Cu, net GND
